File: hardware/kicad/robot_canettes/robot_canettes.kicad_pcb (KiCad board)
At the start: 4 copper layers, 89.7 x 67.6 mm, 116 parts, among them J1 Conn_01x04_Pin, J10 Conn_01x06, J11 Conn_01x06, J2 Conn_01x06, J3 C573320, J4 USB_C_Receptacle_USB2.0_16P, J5 Conn_01x02_Pin, J6 Conn_01x03, J7 Conn_01x06, J8 Conn_01x06, J9 Conn_01x04_Pin, Q1 2N7002, Q2 Q_PMOS, Q5 Q_PNP_CurrentMirror, U1 STM32G431RBTx, U2 MPU-6050, U3 DRV8833PWP, U4 AP2112K-3.3, U5 bq27220, U6 SN74AHCT1G125DBVR, U9 BQ25896RTWR, Y1 16M

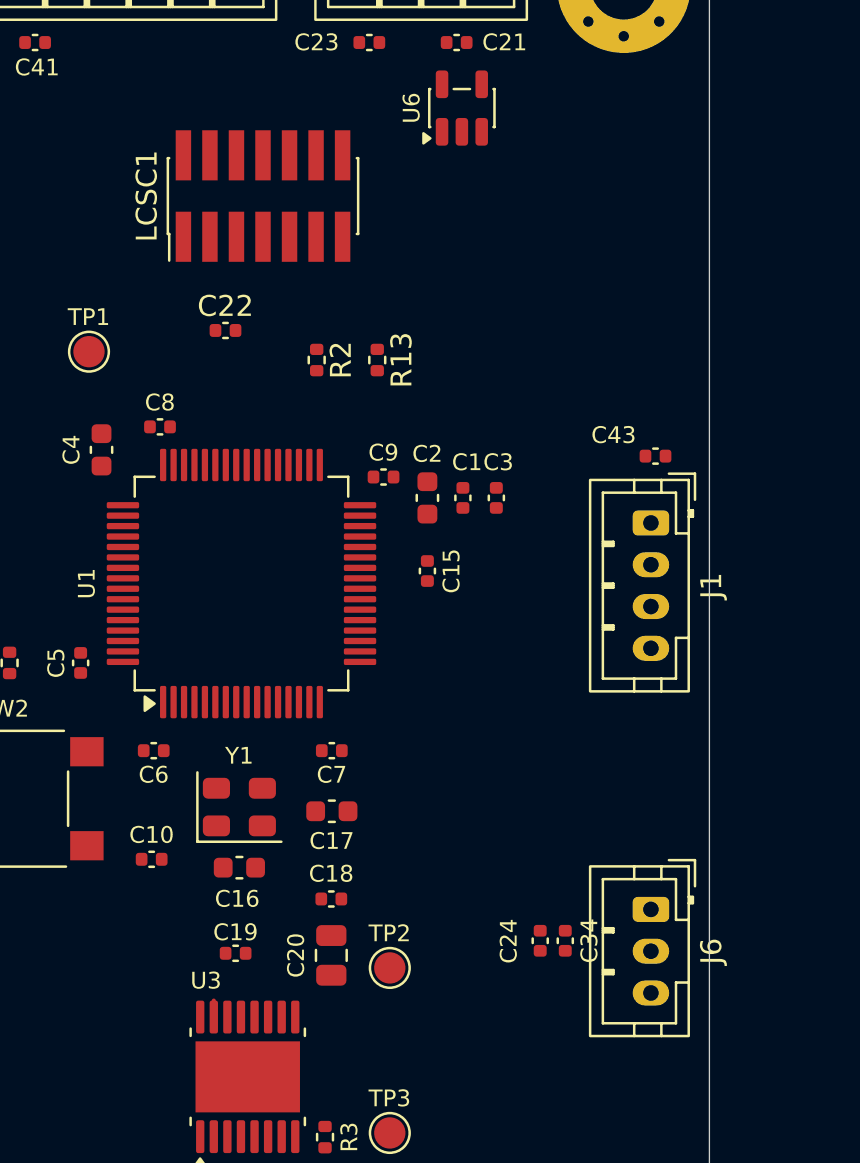
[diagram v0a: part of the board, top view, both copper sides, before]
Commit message: Mise a jour du projet, correction du nom de la feuille sensors
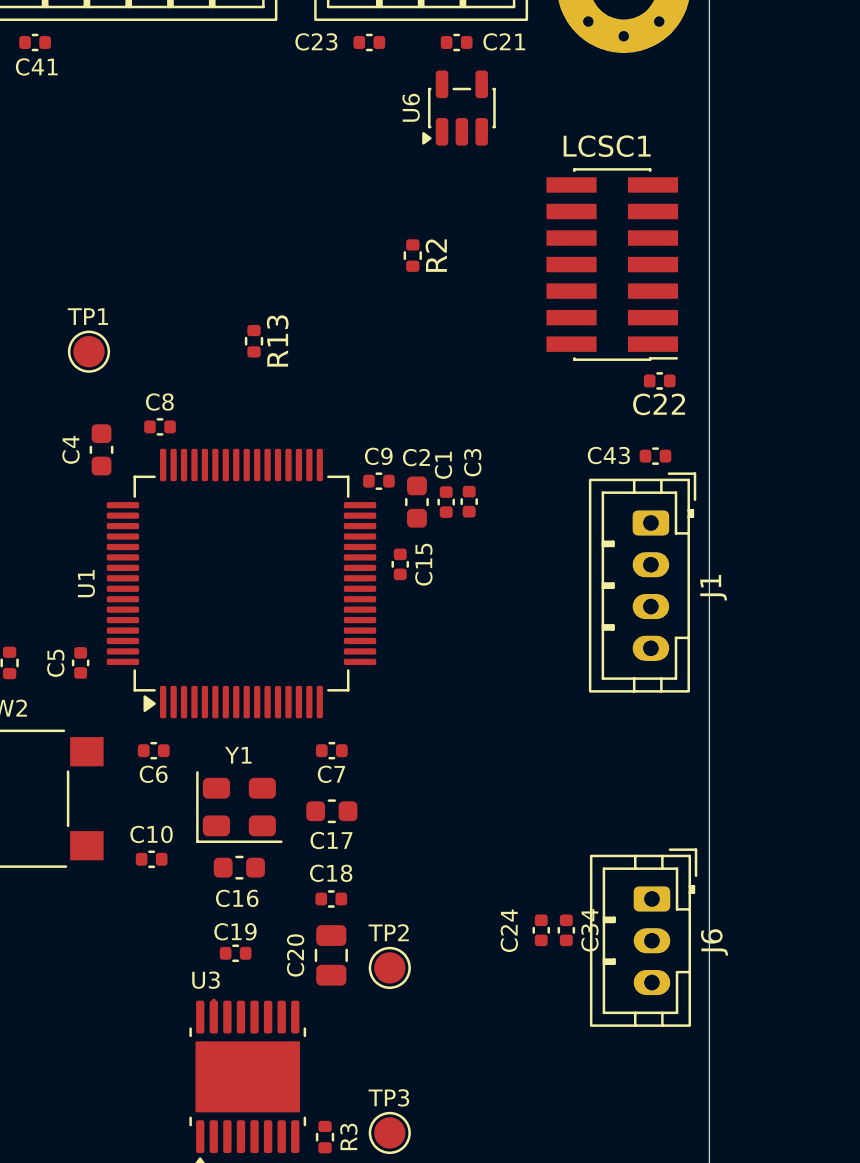
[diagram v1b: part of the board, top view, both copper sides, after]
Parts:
- moved C22 20.9 mm to (-451.6, 117.2), turned to 180 degrees
- moved LCSC1 17.0 mm to (-453.9, 111.6), turned to 180 degrees
- moved R2 6.79 mm to (-463.4, 111.2)
- moved R13 5.97 mm to (-471.0, 115.3)
- moved C15 1.34 mm to (-464.0, 126.0)
- moved C3 1.31 mm to (-460.7, 123.0)
- moved C1 0.82 mm to (-461.8, 123.0)
- moved C2 0.54 mm to (-463.2, 123.0)
- moved C24 0.50 mm to (-457.2, 143.5)
- moved C34 0.50 mm to (-456.1, 143.5)
- moved J6 0.50 mm to (-451.9, 142.0)
- moved C9 0.30 mm to (-465.0, 122.0)

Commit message: Description de vos modifications
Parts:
- removed the H102 at (3.48, 3.48)
- removed the H103 at (3.48, 11.4)
- removed the H104 at (3.48, 19.4)
- moved R13 615.0 mm to (142.9, 78.8)
- moved R21 614.7 mm to (86.4, 98.4), turned to 180 degrees
- moved R14 612.9 mm to (88.2, 99.7)
- moved R10 612.3 mm to (93.3, 113.6)
- moved C13 610.3 mm to (113.6, 93.0)
- moved C25 609.9 mm to (95.5, 77.9)
- moved R1 609.8 mm to (126.3, 98.7)
- moved D2 609.3 mm to (80.5, 103.0)
- moved JP1 608.9 mm to (85.0, 80.4)
- moved R11 608.8 mm to (87.1, 103.8)
- moved R6 608.8 mm to (89.4, 103.8)
- moved R7 608.8 mm to (91.6, 103.8)
- moved C11 608.4 mm to (113.6, 90.8)
- moved R24 608.4 mm to (86.1, 84.6)
- moved R2 608.4 mm to (144.1, 78.8)
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
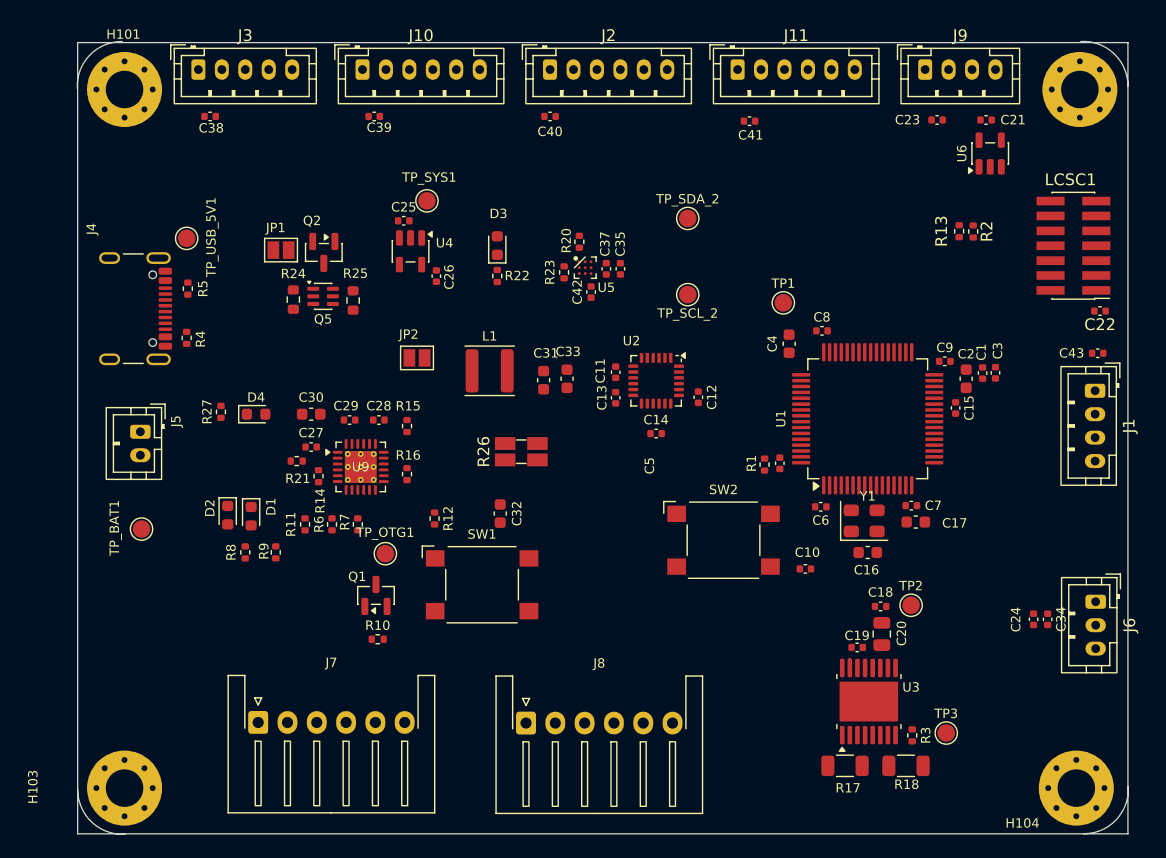
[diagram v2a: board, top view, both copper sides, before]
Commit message: Mise à jour de l'emplacement des composants
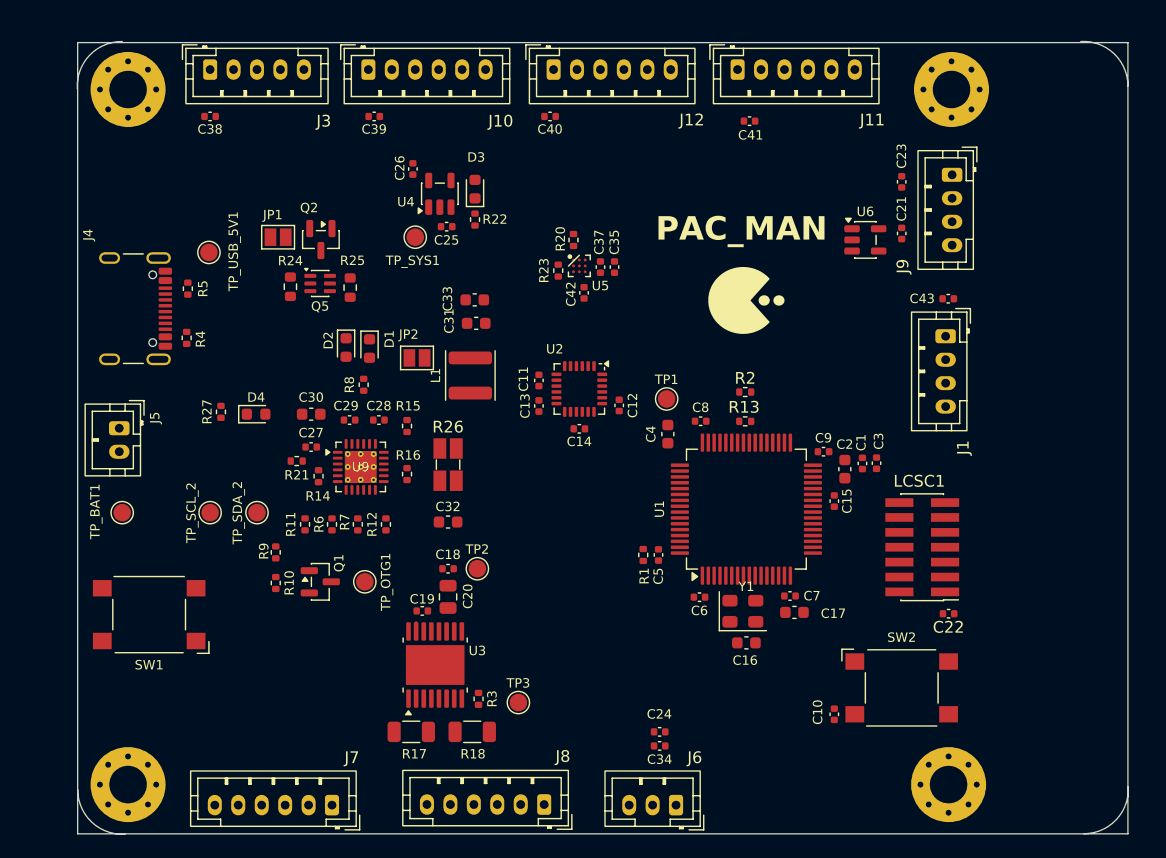
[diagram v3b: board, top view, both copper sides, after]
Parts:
- added G***: LOGO, LOGO, F.Cu at (124.8, 84.8)
- J7, J8: footprint Connector_JST:JST_XH_S6B-XH-A-1_1x06_P2.50mm_Horizontal -> Connector_JST:JST_PH_B6B-PH-K_1x06_P2.00mm_Vertical
- moved TP_SCL_2 44.8 mm to (79.0, 102.8), turned to -90 degrees
- moved TP_SDA_2 44.5 mm to (83.0, 102.8), turned to 90 degrees
- moved J6 39.8 mm to (118.8, 127.8), turned to 180 degrees
- moved C19 37.2 mm to (97.1, 111.2)
- moved C20 37.1 mm to (99.3, 110.0)
- moved TP2 37.1 mm to (101.8, 107.6)
- moved R3 37.1 mm to (101.9, 118.7)
- moved U3 37.1 mm to (98.2, 115.8)
- moved R18 37.1 mm to (101.4, 121.5)
- moved R17 37.1 mm to (96.2, 121.5)
- moved C18 37.0 mm to (99.3, 107.6)
- moved TP3 36.6 mm to (105.3, 119.0)
- moved C34 34.8 mm to (117.3, 122.7), turned to 180 degrees
- moved C24 33.3 mm to (117.3, 121.5), turned to 180 degrees
- moved C22 28.9 mm to (142.0, 111.4)
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- renumbered J2 to J12
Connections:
- C1 pad 2: <NO NET> -> GND
- C10 pad 2: <NO NET> -> GND
- C11 pad 2: <NO NET> -> GND
- C12 pad 2: <NO NET> -> GND
- C13 pad 2: <NO NET> -> GND
- C14 pad 2: <NO NET> -> GND
- C15 pad 2: <NO NET> -> GND
- C16 pad 2: <NO NET> -> GND
- C17 pad 2: <NO NET> -> GND
- C19 pad 1: <NO NET> -> GND
- C2 pad 2: <NO NET> -> GND
- C20 pad 2: <NO NET> -> GND
- C22 pad 2: <NO NET> -> GND
- C23 pad 1: <NO NET> -> GND
- C24 pad 2: <NO NET> -> GND
- C25 pad 2: <NO NET> -> GND
- C26 pad 2: <NO NET> -> GND
- C27 pad 2: <NO NET> -> GND
- C3 pad 2: <NO NET> -> GND
- C30 pad 1: <NO NET> -> GND
- C31 pad 2: <NO NET> -> GND
- C32 pad 2: <NO NET> -> GND
- C33 pad 2: <NO NET> -> GND
- C34 pad 2: <NO NET> -> GND
- C38 pad 2: <NO NET> -> GND
- C39 pad 2: <NO NET> -> GND
- C4 pad 2: <NO NET> -> GND
- C40 pad 2: <NO NET> -> GND
- C41 pad 2: <NO NET> -> GND
- C42 pad 1: <NO NET> -> GND
- C5 pad 2: <NO NET> -> GND
- C6 pad 2: <NO NET> -> GND
- C7 pad 2: <NO NET> -> GND
- C8 pad 2: <NO NET> -> GND
- C9 pad 2: <NO NET> -> GND
- H101 pad 1: <NO NET> -> GND
- J1 pad 4: <NO NET> -> GND
- J3 pad 2: <NO NET> -> GND
- J5 pad 1: <NO NET> -> GND
- J6 pad 1: <NO NET> -> GND
- J8 pad 2: <NO NET> -> GND
- J9 pad 3: <NO NET> -> GND
- LCSC1 pad 11: <NO NET> -> GND
- LCSC1 pad 5: <NO NET> -> GND
- LCSC1 pad 7: <NO NET> -> GND
- Q1 pad 2: <NO NET> -> GND
- R1 pad 2: <NO NET> -> GND
- R10 pad 2: <NO NET> -> GND
- R16 pad 2: <NO NET> -> GND
- R17 pad 2: <NO NET> -> GND
- R18 pad 2: <NO NET> -> GND
- R22 pad 2: <NO NET> -> GND
- R24 pad 2: <NO NET> -> GND
- R25 pad 2: <NO NET> -> GND
- R27 pad 2: <NO NET> -> GND
- SW1 pad 1: <NO NET> -> GND
- SW2 pad 1: <NO NET> -> GND
- U1 pad 15: <NO NET> -> GND
- U1 pad 27: <NO NET> -> GND
- U1 pad 31: <NO NET> -> GND
- U1 pad 47: <NO NET> -> GND
- U1 pad 63: <NO NET> -> GND
- U2 pad 11: <NO NET> -> GND
- U2 pad 18: <NO NET> -> GND
- U2 pad 9: <NO NET> -> GND
- U3 pad 13: <NO NET> -> GND
- U3 pad 17: <NO NET> -> GND
- U4 pad 2: <NO NET> -> GND
- U5 pad B2: <NO NET> -> GND
- U9 pad 17: <NO NET> -> GND
- U9 pad 18: <NO NET> -> GND
- U9 pad 25: <NO NET> -> GND
- U9 pad 9: <NO NET> -> GND
- Y1 pad 2: <NO NET> -> GND
- Y1 pad 4: <NO NET> -> GND
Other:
- board text added: "PAC_MAN"

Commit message: Modification du projet
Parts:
- moved C40 17.0 mm to (125.0, 69.0)
- moved C41 15.5 mm to (109.5, 69.0)
- moved C22 4.85 mm to (144.0, 107.0), turned to 90 degrees
- moved R24 2.40 mm to (84.0, 82.0)
- moved C35 2.30 mm to (114.0, 84.1)
- moved C37 2.30 mm to (112.8, 84.1)
- moved C42 2.30 mm to (111.4, 86.3)
- moved R20 2.30 mm to (110.5, 81.8)
- moved R23 2.30 mm to (109.2, 84.4)
- moved U5 2.30 mm to (111.0, 84.0)
- moved R2 2.22 mm to (123.0, 94.0), turned to -90 degrees
- moved Q5 1.25 mm to (87.2, 83.0)
- moved R25 1.12 mm to (90.0, 83.0)
- moved C17 1.09 mm to (128.0, 112.0)
- moved R13 1.07 mm to (125.0, 94.0), turned to -90 degrees
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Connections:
- H102 pad 1: <NO NET> -> GND
- H103 pad 1: <NO NET> -> GND
- H104 pad 1: <NO NET> -> GND
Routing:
- net /MCU/MOTOR_A_IN2: track 0.79 -> 0.00 mm
- added copper zone on In1.Cu, net GND
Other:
- board size 89.7 x 67.6 mm -> 78 x 68 mm

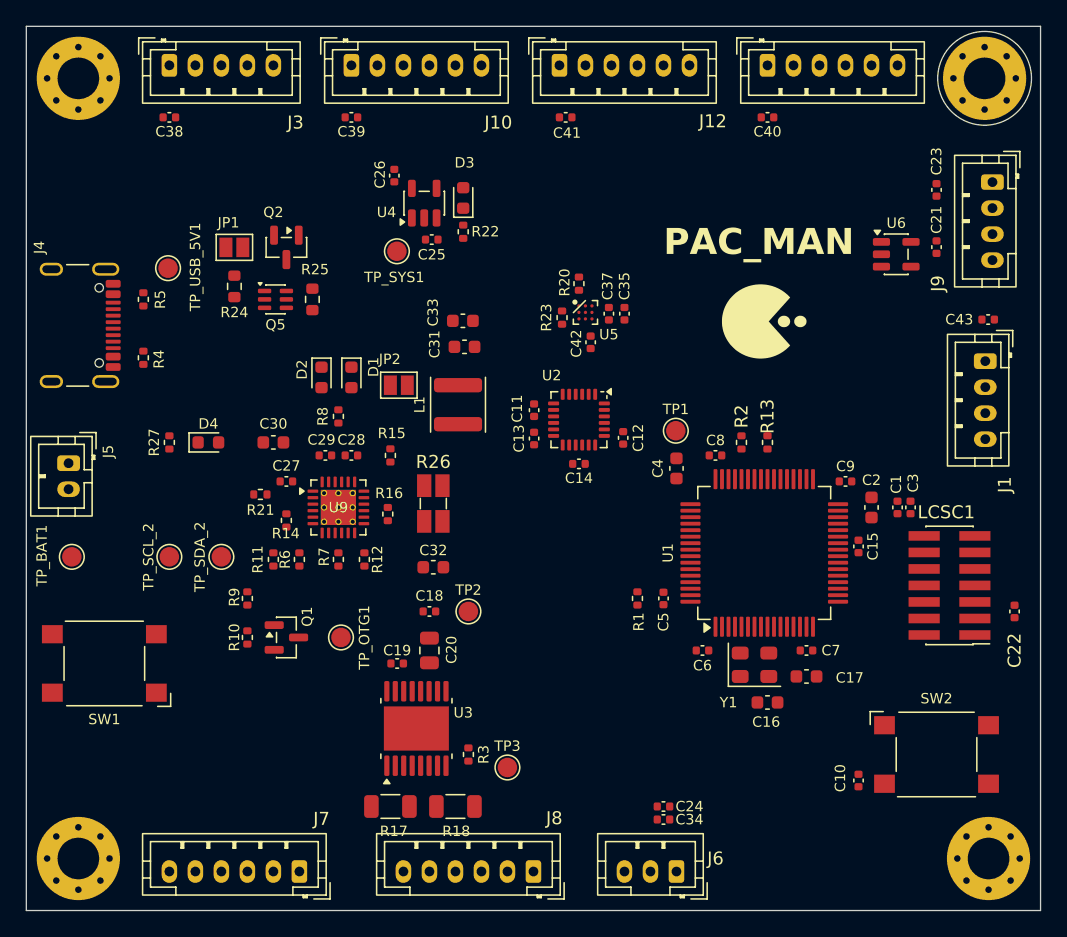
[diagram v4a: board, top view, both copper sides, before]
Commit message: Mise à jour PCB depuis le zip
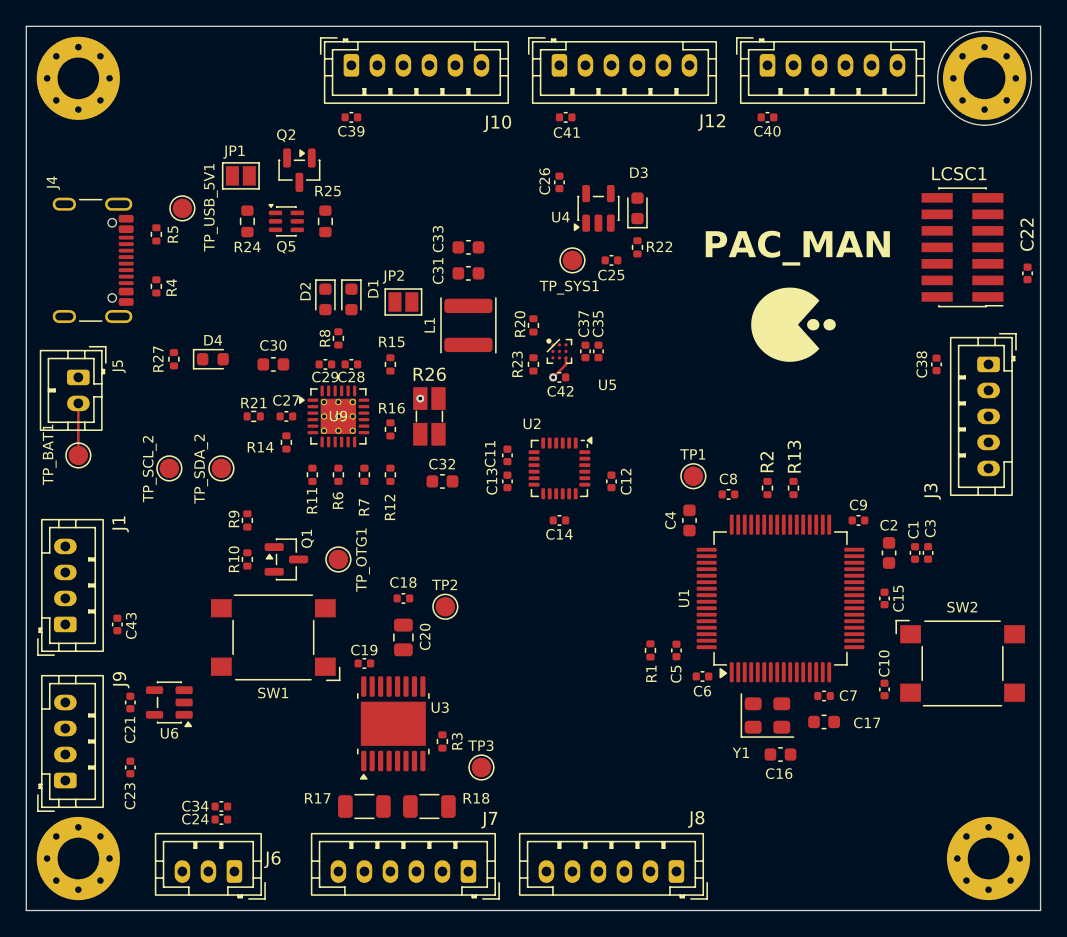
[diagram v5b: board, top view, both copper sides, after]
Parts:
- H102: value MountingHole_Pad -> GND
- moved J9 84.9 mm to (71.0, 120.0), turned to 90 degrees
- moved C23 76.3 mm to (76.0, 119.0), turned to -90 degrees
- moved J1 73.6 mm to (71.0, 108.0), turned to 90 degrees
- moved C21 71.2 mm to (76.0, 114.0), turned to 90 degrees
- moved C43 71.0 mm to (75.0, 108.0), turned to -90 degrees
- moved J3 67.1 mm to (142.0, 88.0), turned to -90 degrees
- moved U6 65.7 mm to (79.0, 114.0), turned to 180 degrees
- moved C38 62.0 mm to (138.0, 88.0), turned to -90 degrees
- moved C24 34.0 mm to (83.0, 123.0), turned to 0 degrees
- moved C34 34.0 mm to (83.0, 122.0), turned to 0 degrees
- moved J6 34.0 mm to (84.0, 127.0)
- moved C22 26.0 mm to (145.0, 81.0)
- moved LCSC1 26.0 mm to (140.0, 79.0)
- moved C25 13.9 mm to (113.0, 80.0)
- moved TP_SYS1 13.5 mm to (110.0, 80.0)
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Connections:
- J10 pad 2: <NO NET> -> GND
- J11 pad 2: <NO NET> -> GND
- J12 pad 2: <NO NET> -> GND
- J7 pad 2: <NO NET> -> GND
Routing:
- net +BATT: track 0.00 -> 43.6 mm, vias 0 -> 2
- added copper zone on In2.Cu, net +3.3V
- added copper zone on In2.Cu, net USB_5V
- added copper zone on In2.Cu, net VBUS

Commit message: Update PCB routing and placement
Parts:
- moved C15 1.00 mm to (134.0, 107.0)
- moved C27 0.52 mm to (87.5, 92.0)
- moved R21 0.52 mm to (85.0, 92.0)
- moved R20 0.35 mm to (106.8, 84.8)
- moved TP1 0.34 mm to (119.0, 96.8)
- moved U5 0.25 mm to (109.0, 87.2)
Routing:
- net /MCU/I2C2_SCL: track 0.00 -> 81.0 mm, vias 0 -> 2
- net /MCU/I2C2_SDA: track 0.00 -> 60.4 mm
- net GND: track 0.00 -> 49.0 mm, vias 0 -> 56
- net /MCU/USART1_RX: track 0.00 -> 40.4 mm, vias 0 -> 2
- net /MCU/SWCLK: track 0.00 -> 37.2 mm, vias 0 -> 2
- net /MCU/GAUGE_INT: track 0.00 -> 36.7 mm, vias 0 -> 3
- net /MCU/USART1_TX: track 0.00 -> 34.1 mm, vias 0 -> 2
- net /MCU/SWDIO: track 0.00 -> 31.4 mm, vias 0 -> 2
- net +3.3V: track 0.00 -> 18.5 mm, vias 0 -> 25
- net VBUS: track 0.02 -> 7.63 mm, vias 0 -> 9

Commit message: Update robot PCB
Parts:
- moved C22 5.47 mm to (141.0, 84.8), turned to 180 degrees
- moved C5 1.25 mm to (116.8, 110.0)
- moved C43 1.01 mm to (75.2, 109.0)
- moved C39 1.00 mm to (94.0, 69.0)
- moved R13 0.77 mm to (127.0, 96.7)
- moved R2 0.77 mm to (125.0, 96.7)
- moved R1 0.75 mm to (115.2, 110.0)
- moved C27 0.56 mm to (87.2, 92.5)
- moved R21 0.55 mm to (84.7, 92.5)
- moved C18 0.25 mm to (97.0, 106.2)
- moved R4 0.25 mm to (78.2, 82.0)
- moved R5 0.25 mm to (78.2, 78.0)
- moved C8 0.23 mm to (121.8, 98.0)
- moved TP_USB_5V1 0.12 mm to (80.1, 76.0)
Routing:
- net /MCU/I2C3_SCL: track 0.00 -> 113.2 mm, vias 0 -> 2
- net /MCU/SERVO1_PWM: track 0.00 -> 78.8 mm, vias 0 -> 2
- net /MCU/ESP32_RX: track 0.00 -> 70.6 mm, vias 0 -> 2
- net /MCU/NRST: track 0.00 -> 66.3 mm, vias 0 -> 5
- net /MCU/ESP32_TX: track 0.00 -> 62.9 mm, vias 0 -> 2
- net /MCU/I2C3_SDA: track 0.00 -> 60.5 mm, vias 0 -> 6
- net GND: track 49.0 -> 97.6 mm, vias 56 -> 90
- net /MCU/NEOPIXEL: track 0.00 -> 43.0 mm, vias 0 -> 2
- net +3.3V: track 18.5 -> 52.3 mm, vias 25 -> 44
- net SYS: track 0.00 -> 30.4 mm
- net /MCU/APDS_INT: track 0.00 -> 18.6 mm, vias 0 -> 2
- net VBUS: track 7.63 -> 22.9 mm, vias 9 -> 20
- net /MCU/NP_5V: track 0.00 -> 7.36 mm, vias 0 -> 1
- net USB_5V: track 0.46 -> 5.97 mm, vias 0 -> 4
- net +BATT: track 43.4 -> 47.4 mm
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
